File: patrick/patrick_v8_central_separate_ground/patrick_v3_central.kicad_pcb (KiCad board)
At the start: 2 copper layers, 53.1 x 53.9 mm, 32 parts, among them J1 Conn_02x05_Counter_Clockwise, J10 61300311121, J2 Conn_02x05_Counter_Clockwise, J3 Conn_02x05_Counter_Clockwise, J4 Conn_02x05_Counter_Clockwise, J5 Conn_02x05_Counter_Clockwise, J6 DM3CS-SF, J7 61300211121, J8 Conn_01x03, Q1 RUE002N02TL, Q2 RUE002N02TL, Q3 RUE002N02TL, U1 ICM-20948, U2 MCP1702T-1802E_CB, U3 BL652-SA-01, U4 PCA9685PW_Q900,118, U5 PCA9685PW_Q900,118, U6 MPM3610GQV-Z

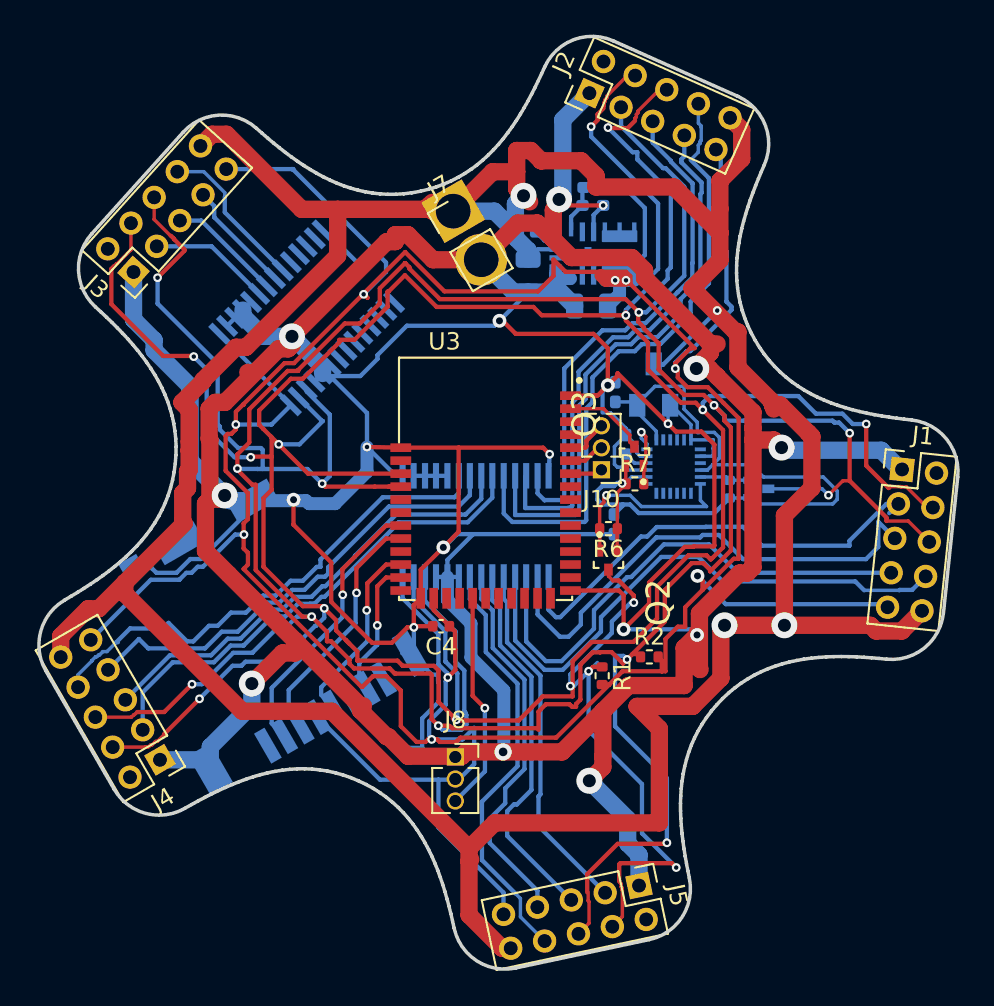
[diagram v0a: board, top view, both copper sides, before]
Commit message: separate gnd
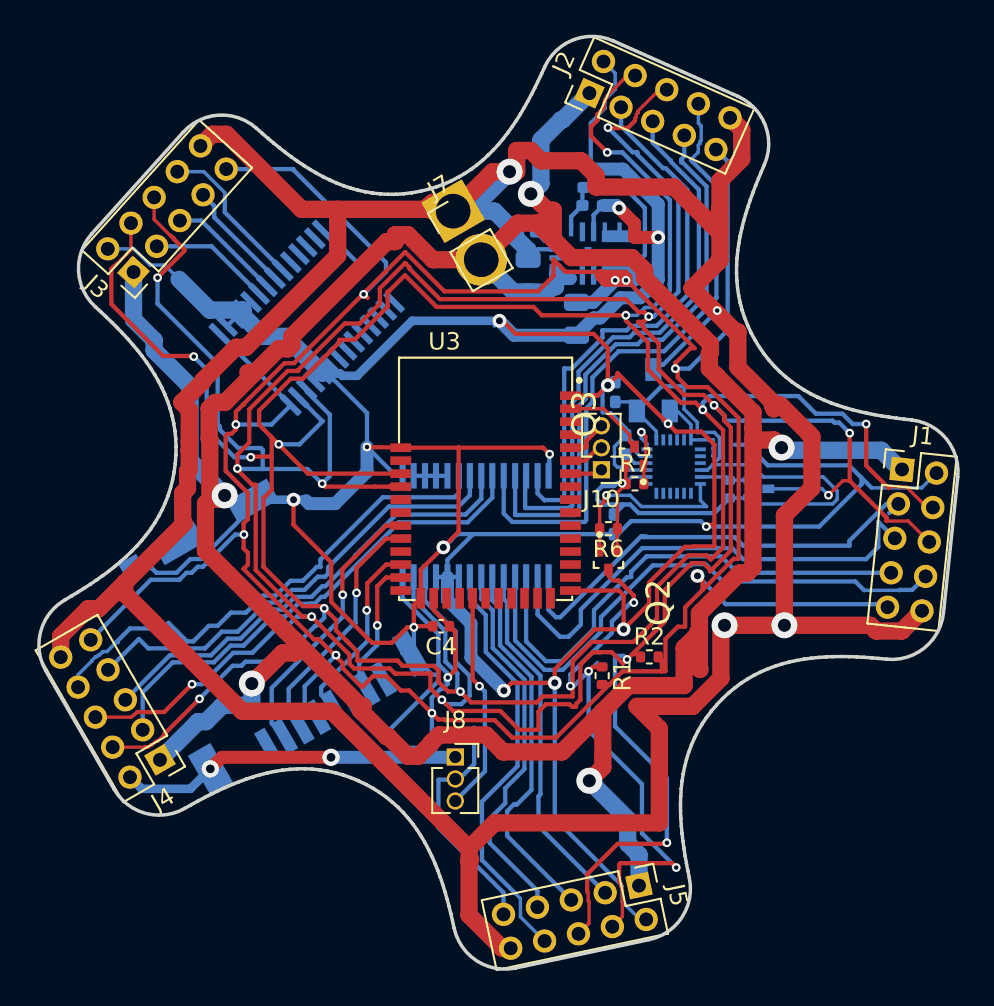
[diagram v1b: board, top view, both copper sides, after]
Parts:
- moved C1 1.12 mm to (114.1, 99.3), turned to 270 degrees
- moved U2 0.33 mm to (118.5, 103.4)
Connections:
- C1 pad 2: GND -> GND2
- C2 pad 1: GND -> GND2
- C4 pad 2: GND -> GND2
- C5 pad 1: GND -> GND2
- C6 pad 1: GND -> GND2
- J1 pad 2: Net-(J1-Pad2) -> GND2
- J2 pad 2: Net-(J2-Pad2) -> GND2
- J3 pad 2: Net-(J3-Pad2) -> GND2
- J4 pad 2: Net-(J4-Pad2) -> GND2
- J5 pad 2: Net-(J5-Pad2) -> GND2
- J6 pad 6: GND -> GND2
- J6 pad S1: GND -> GND2
- J6 pad S2: GND -> GND2
- J6 pad S3: GND -> GND2
- J6 pad S5: GND -> GND2
- J8 pad 1: GND -> GND2
- R4 pad 1: GND -> GND2
- U1 pad 11: GND -> GND2
- U1 pad 18: GND -> GND2
- U1 pad 20: GND -> Net-(U1-Pad20)
- U1 pad 9: GND -> GND2
- U2 pad 1: GND -> GND2
- U3 pad 1: GND -> GND2
- U3 pad 16: GND -> GND2
- U3 pad 27: GND -> GND2
- U3 pad 39: GND -> GND2
- U4 pad 1: GND -> GND2
- U4 pad 14: GND -> GND2
- U4 pad 2: GND -> GND2
- U4 pad 23: GND -> GND2
- U4 pad 24: GND -> GND2
- U4 pad 25: GND -> GND2
- U4 pad 3: GND -> GND2
- U4 pad 4: GND -> GND2
- U4 pad 5: GND -> GND2
- U5 pad 14: GND -> GND2
- U5 pad 2: GND -> GND2
- U5 pad 23: GND -> GND2
- U5 pad 24: GND -> GND2
- U5 pad 25: GND -> GND2
- U5 pad 3: GND -> GND2
- U5 pad 4: GND -> GND2
- U5 pad 5: GND -> GND2
- U6 pad 3: GND -> GND2
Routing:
- net GND2: track 0.00 -> 308.1 mm, vias 0 -> 16
- net GND: track 384.1 -> 174.7 mm, vias 19 -> 5
- net +3V3: track 218.8 -> 215.4 mm, vias 9 -> 10
- net /SDA: track 218.6 -> 216.8 mm
- net /SCL: track 222.7 -> 221.3 mm
- net /SMA16_SIG: track 31.0 -> 31.9 mm
- net /SMA13_SIG: track 36.1 -> 36.8 mm
- net /SMA15_SIG: track 31.7 -> 32.4 mm
- net /SMA14_SIG: track 32.7 -> 33.3 mm
- net /SMA11_SIG: track 28.9 -> 28.4 mm

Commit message: separate gnd
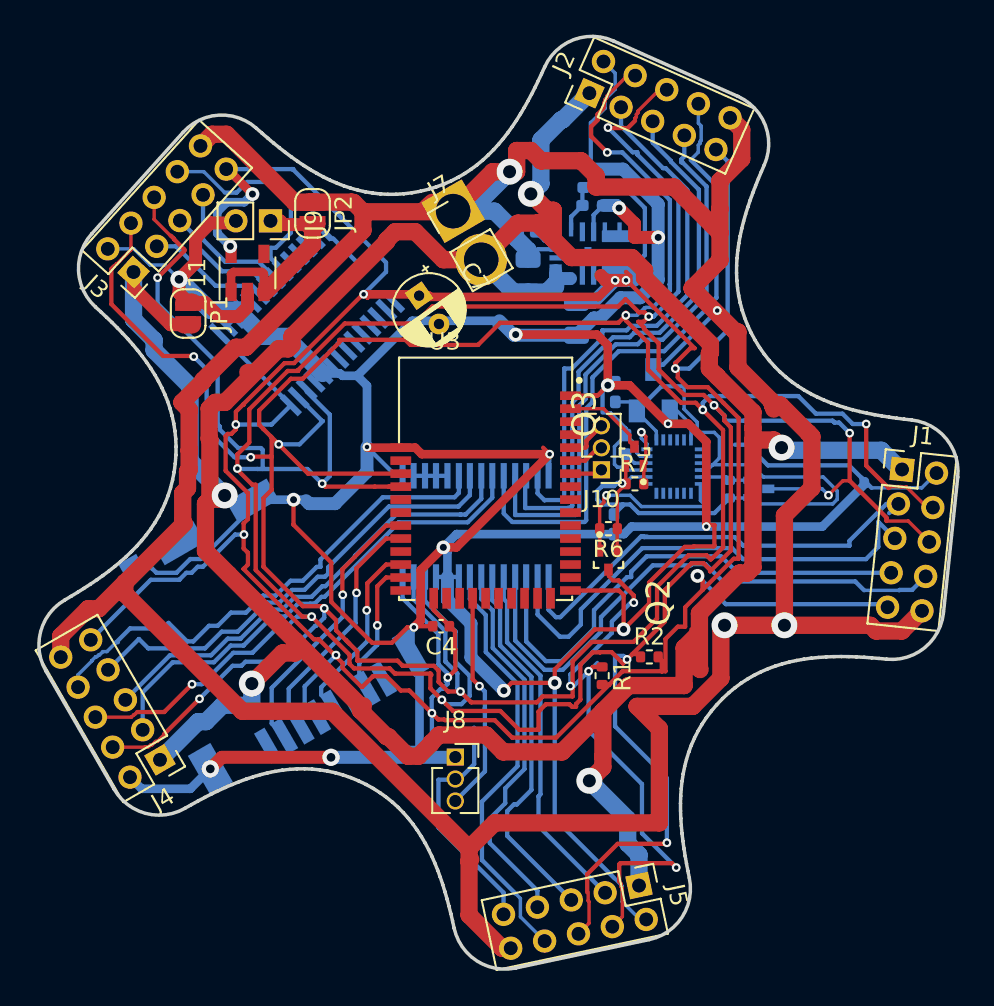
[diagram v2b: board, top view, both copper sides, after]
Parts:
- added 11: V_REG_SPX3819-SOT23-5, Package_TO_SOT_SMD:SOT-23-5, F.Cu at (95.1, 96.7)
- added C7: CP1_Small, Capacitor_THT:CP_Radial_D4.0mm_P2.00mm, F.Cu at (105.0, 98.0)
- added J9: Conn_01x02, Connector_PinSocket_2.00mm:PinSocket_1x02_P2.00mm_Vertical, F.Cu at (96.4, 93.7)
- added JP1: Jumper_NO_Small, Jumper:SolderJumper-2_P1.3mm_Open_RoundedPad1.0x1.5mm, F.Cu at (91.7, 99.0)
- added JP2: Jumper_NO_Small, Jumper:SolderJumper-2_P1.3mm_Open_RoundedPad1.0x1.5mm, F.Cu at (98.8, 93.2)
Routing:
- net Net-(11-Pad1): track 0.00 -> 11.6 mm
- net GND2: track 308.1 -> 316.1 mm, vias 16 -> 17
- net GND: track 174.7 -> 179.6 mm
- net /SMA17_SIG: track 9.11 -> 12.7 mm
- net +3V3: track 215.4 -> 218.6 mm, vias 10 -> 12
- net /SCL: track 221.3 -> 218.9 mm
- net /SDA: track 216.8 -> 214.7 mm
- net +8V: track 197.2 -> 199.3 mm
- net /SMA18_SIG: track 6.53 -> 7.66 mm
- net /SMA19_SIG: track 6.59 -> 7.53 mm
